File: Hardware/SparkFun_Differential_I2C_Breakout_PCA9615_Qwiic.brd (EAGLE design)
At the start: 43.2 x 27.9 mm, 49 parts, among them J1 QWIIC_RIGHT_ANGLE, J2 QWIIC_RIGHT_ANGLE, J3 RJ45, J7 RJ45, U1 PCA9615, U2 3.3V

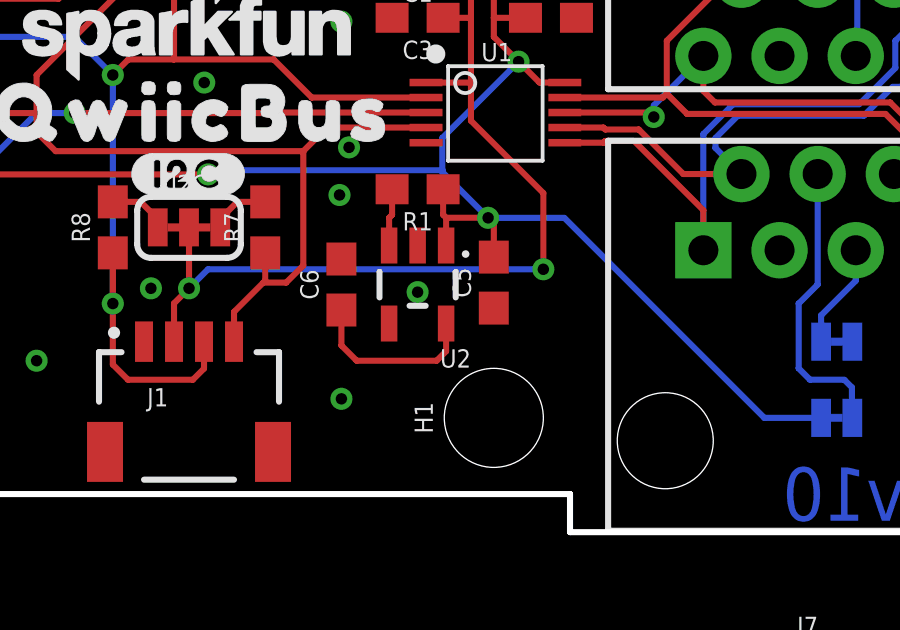
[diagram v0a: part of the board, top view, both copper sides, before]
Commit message: updating net name to fix VDD_A issue
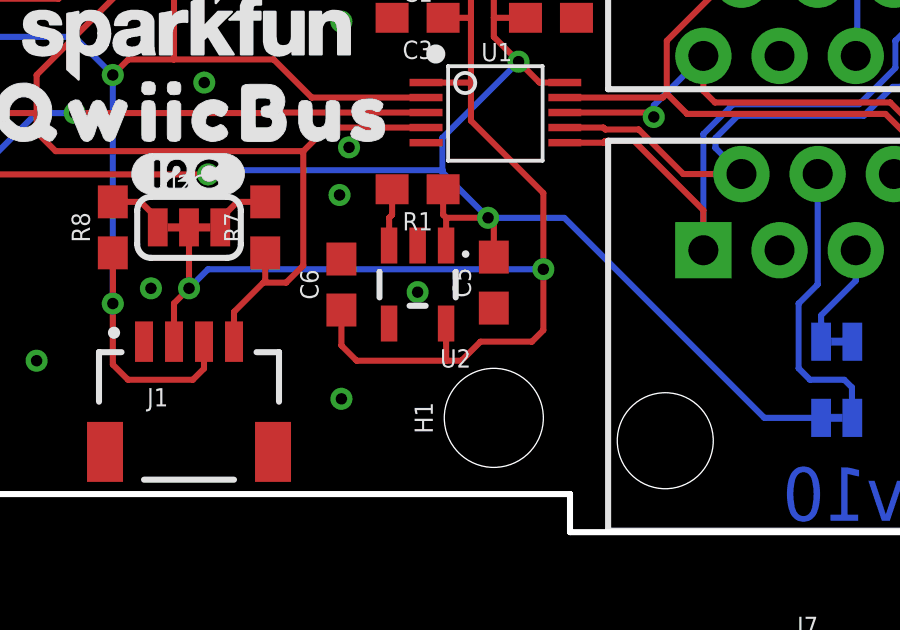
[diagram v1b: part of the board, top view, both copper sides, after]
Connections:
- removed net VCC_1: C6.1, U2.5
- net VDD_A: now also C6.1, U2.5
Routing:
- net VDD_A: track 60.2 -> 72.0 mm
- net VCC_1: track 5.94 -> 0.00 mm
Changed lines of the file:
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@@
 <wire x1="24.511" y1="11.303" x2="22.098" y2="13.716" width="0.2032" layer="1"/>
 <wire x1="22.098" y1="14.986" x2="22.098" y2="13.716" width="0.2032" layer="1"/>
+<contactref element="C6" pad="1"/>
+<contactref element="U2" pad="5"/>
+<wire x1="17.78" y1="7.405" x2="17.78" y2="6.223" width="0.2032" layer="1"/>
+<wire x1="17.78" y1="6.223" x2="18.288" y2="5.715" width="0.2032" layer="1"/>
+<wire x1="21.27" y1="6.03" x2="21.27" y2="6.35" width="0.2032" layer="1"/>
+<wire x1="21.27" y1="6.35" x2="21.27" y2="6.9549" width="0.2032" layer="1"/>
+<wire x1="22.4155" y1="6.35" x2="24.13" y2="6.35" width="0.2032" layer="1"/>
+<wire x1="24.13" y1="6.35" x2="24.511" y2="6.731" width="0.2032" layer="1"/>
+<wire x1="24.511" y1="6.731" x2="24.511" y2="8.763" width="0.2032" layer="1"/>
+<wire x1="18.288" y1="5.715" x2="21.2725" y2="5.715" width="0.2032" layer="1"/>
+<wire x1="21.2725" y1="5.715" x2="21.7805" y2="5.715" width="0.2032" layer="1"/>
+<wire x1="21.7805" y1="5.715" x2="22.4155" y2="6.35" width="0.2032" layer="1"/>
+<wire x1="21.27" y1="6.03" x2="21.27" y2="5.7175" width="0.2032" layer="1"/>
+<wire x1="21.27" y1="5.7175" x2="21.2725" y2="5.715" width="0.2032" layer="1"/>
 </signal>
 <signal name="VDD_B">
@@
 <wire x1="19.47" y1="10.58" x2="19.37" y2="10.48" width="0.2032" layer="1"/>
 </signal>
-<signal name="VCC_1">
-<contactref element="C6" pad="1"/>
-<contactref element="U2" pad="5"/>
-<wire x1="17.78" y1="7.405" x2="17.78" y2="6.223" width="0.2032" layer="1"/>
-<wire x1="17.78" y1="6.223" x2="18.288" y2="5.715" width="0.2032" layer="1"/>
-<wire x1="21.27" y1="6.03" x2="21.27" y2="6.9549" width="0.2032" layer="1"/>
-<wire x1="18.288" y1="5.715" x2="20.955" y2="5.715" width="0.2032" layer="1"/>
-<wire x1="20.955" y1="5.715" x2="21.27" y2="6.03" width="0.2032" layer="1"/>
-</signal>
 </signals>

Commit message: post design review checklist changes
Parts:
- removed JP3, JP4: JUMPER-SMT_2_NC_TRACE_SILK, SparkFun-Jumpers:SMT-JUMPER_2_NC_TRACE_SILK
- added A-B: JUMPER-SMT_2_NO_SILK, SparkFun-Jumpers:SMT-JUMPER_2_NO_SILK
- added GND\, VDD_B, VREG: JUMPER-SMT_2_NC_TRACE_SILK, SparkFun-Jumpers:SMT-JUMPER_2_NC_TRACE_SILK
- added U$16, U$18, U$19: (no value), output:#VDDB#0
- added U$17: (no value), output:#VREG#0
- added U$20, U$21: (no value), output:#GND#0
- added U$22: (no value), SparkFun-Aesthetics:QWIIC_4MM
- J1, J2: value QWIIC_RIGHT_ANGLE -> QWIIC
- U$11: device output:#5V#0 -> output:#A#B#0
- U$5: device output:#5V#0 -> output:#VDDB#0
- moved U$11 19.0 mm to (22.0, 19.1)
- moved C6 6.99 mm to (24.8, 8.32)
- moved FRAME1 6.35 mm to (-16.5, -15.2)
- moved U$5 5.59 mm to (7.37, 10.2), flipped to the bottom
- moved U$15 2.54 mm to (20.6, 7.62)
- moved JP5 2.16 mm to (36.4, 3.81)
- moved JP6 2.16 mm to (36.4, 6.35)
- moved C5 1.27 mm to (21.6, 8.32)
- moved R1 1.27 mm to (19.1, 11.4)
- moved U2 1.27 mm to (19.1, 8.26)
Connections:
- new net GRN: J3.6, J7.6
- new net N$8: U2.1, VREG.2
- new net W_GRN: J3.3, J7.3
- net GND: now also GND\.1; no longer JP4.1
- net N$1: now also VDD_B.2; no longer JP3.2
- net N$2: now also GND\.2; no longer JP4.2
- net VDD_A: now also A-B.1
- net VDD_B: now also A-B.2, VDD_B.1, VREG.1; no longer JP3.1, U2.1
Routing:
- net GRN: track 0.00 -> 20.7 mm
- net W_GRN: track 0.00 -> 19.9 mm
- net VDD_B: track 67.1 -> 73.6 mm, vias 4 -> 5
- net N$8: track 0.00 -> 3.20 mm, vias 0 -> 1
- net VDD_A: track 72.0 -> 69.0 mm, vias 2 -> 3
- net N$2: track 3.65 -> 5.65 mm
- net N$1: track 9.72 -> 11.1 mm
- net N$5: track 9.80 -> 10.9 mm
- net SCL: track 39.0 -> 37.9 mm
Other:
- board text added: "Units in Inches"
